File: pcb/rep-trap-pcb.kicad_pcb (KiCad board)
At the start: 2 copper layers, 141.9 x 37 mm, 39 parts, among them J1 USB4105-GF-A, J2 S2B-PH-K, U1 VL53L4CDV0DH/1, U2 VL53L4CDV0DH/1, U3 VL53L4CDV0DH/1, U4 VL53L4CDV0DH/1, U5 RP2040, U6 MCP73831/OT, U8 AP2112K-3.3

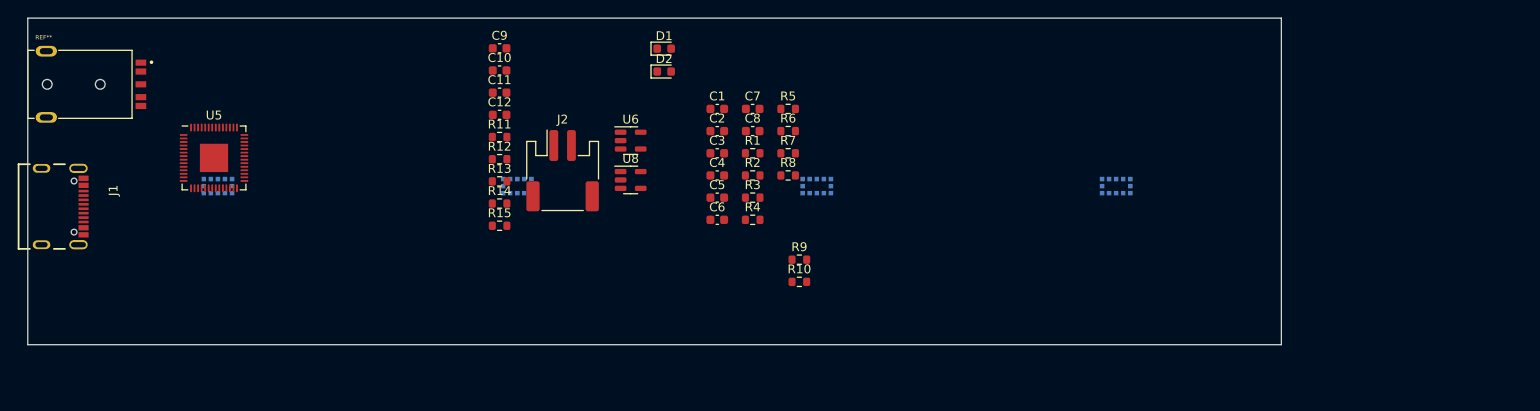
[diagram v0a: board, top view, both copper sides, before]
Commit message: Added pcb design for first prototype
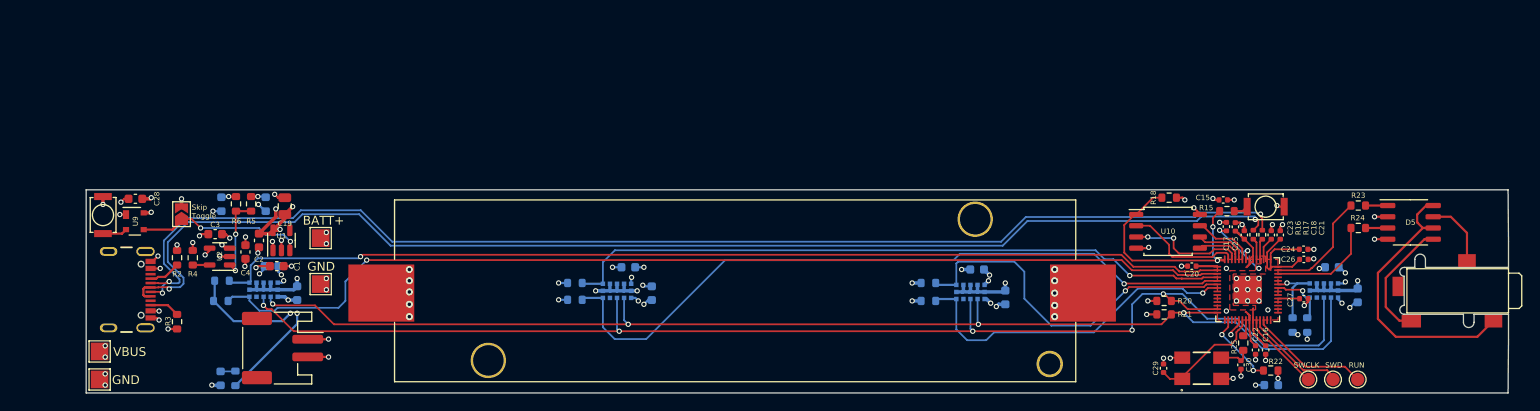
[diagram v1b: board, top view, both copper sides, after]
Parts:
- removed REF**: CUI_SJ-3541AS-SMT-TR-67, SJ-3541AS-SMT-TR-67:CUI_SJ-3541AS-SMT-TR-67
- added BT1: Battery_Cell, 1042P:1042P, F.Cu at (142.6, 90.9)
- added C15: 100n, Capacitor_SMD:C_0402_1005Metric, F.Cu at (197.9, 80.4)
- added C16: 0.1uF, Capacitor_SMD:C_0402_1005Metric, F.Cu at (202.7, 97.4)
- added C17: 0.1uF, Capacitor_SMD:C_0402_1005Metric, F.Cu at (198.2, 83.4)
- added C18: 1uF, Capacitor_SMD:C_0402_1005Metric, F.Cu at (203.3, 84.4)
- added C19: 10uF, Capacitor_SMD:C_0805_2012Metric, F.Cu at (91.7, 81.1)
- added C20: 0.1uF, Capacitor_SMD:C_0402_1005Metric, F.Cu at (194.3, 87.9)
- added C21: 1uF, Capacitor_SMD:C_0402_1005Metric, F.Cu at (204.3, 84.4)
- added C22: 0.1uF, Capacitor_SMD:C_0402_1005Metric, F.Cu at (201.5, 97.4)
- added C23: 0.1uF, Capacitor_SMD:C_0402_1005Metric, F.Cu at (200.3, 84.4)
- added C24: 0.1uF, Capacitor_SMD:C_0402_1005Metric, F.Cu at (207.0, 86.0)
- added C25: 0.1uF, Capacitor_SMD:C_0402_1005Metric, F.Cu at (199.3, 83.4)
- added C26: 0.1uF, Capacitor_SMD:C_0402_1005Metric, F.Cu at (207.0, 87.1)
- added C27: 0.1uF, Capacitor_SMD:C_0402_1005Metric, F.Cu at (207.0, 91.6)
- added C28: 0.1uF, Capacitor_SMD:C_0603_1608Metric, F.Cu at (74.8, 80.3)
- added C29: 27p, Capacitor_SMD:C_0402_1005Metric, F.Cu at (191.1, 99.4)
- added C30: 27p, Capacitor_SMD:C_0402_1005Metric, F.Cu at (199.9, 99.1)
- added D3: GREEN, LED_SMD:LED_0603_1608Metric, B.Cu at (84.5, 80.9)
- added D4: LED_RED, LED_SMD:LED_0603_1608Metric, B.Cu at (203.3, 101.3)
- added D5: ELD207, Package_SO:SO-8_3.9x4.9mm_P1.27mm, F.Cu at (219.1, 82.9)
- added J3: USB4105-GF-A, USB4105-GF-A:GCT_USB4105-GF-A, F.Cu at (71.8, 90.5)
- added J4: VBUS, TestPoint:TestPoint_Pad_2.0x2.0mm, F.Cu at (70.7, 97.5)
- added J5: SJ2-25773B-SMT-TR, SJ-25773B-SMT:CUI_SJ2-25773B-SMT-TR, F.Cu at (224.4, 90.7)
- added J6: S2B-PH-K/DNP, Connector_JST:JST_PH_S2B-PH-SM4-TB_1x02-1MP_P2.00mm_Horizontal, F.Cu at (91.4, 97.2)
- added J7: GND, TestPoint:TestPoint_Pad_2.0x2.0mm, F.Cu at (70.7, 100.7)
- added JP1: SolderJumper_2_Open, Jumper:SolderJumper-2_P1.3mm_Open_TrianglePad1.0x1.5mm, F.Cu at (80.0, 82.0)
- added R16: 27, Resistor_SMD:R_0402_1005Metric, F.Cu at (201.3, 84.3)
- added R17: 27, Resistor_SMD:R_0402_1005Metric, F.Cu at (202.3, 84.3)
- added R18: 10k/DNP, Resistor_SMD:R_0603_1608Metric, F.Cu at (191.8, 80.1)
- added R20: 10k, Resistor_SMD:R_0603_1608Metric, F.Cu at (191.2, 91.8)
- added R21: 10k, Resistor_SMD:R_0603_1608Metric, F.Cu at (191.2, 93.3)
- added R22: 1k, Resistor_SMD:R_0603_1608Metric, F.Cu at (203.3, 99.7)
- added R23: 220, Resistor_SMD:R_0603_1608Metric, F.Cu at (213.2, 81.0)
- added R24: 220, Resistor_SMD:R_0603_1608Metric, F.Cu at (213.2, 83.6)
- added R25: 1k, Resistor_SMD:R_0603_1608Metric, F.Cu at (200.2, 96.6)
- added SW1: SW_Push, SKRKAEE020:SKRKAEE020, F.Cu at (202.7, 81.2)
- added SW2: SW_Push, SKRKAEE020:SKRKAEE020, F.Cu at (71.1, 82.1)
- added TP1: TP_SWCLK, TestPoint:TestPoint_Pad_D1.5mm, F.Cu at (207.5, 100.7)
- added TP2: TP_SWD, TestPoint:TestPoint_Pad_D1.5mm, F.Cu at (210.3, 100.7)
- added TP3: TestPoint, TestPoint:TestPoint_Pad_D1.5mm, F.Cu at (213.1, 100.7)
- added U10: W25Q128JVS, Package_SO:SOIC-8_5.23x5.23mm_P1.27mm, F.Cu at (191.6, 83.9)
- added U9: MAX6816, Package_TO_SOT_SMD:SOT-143, F.Cu at (74.7, 82.8)
- added Y3: ABMM2-12.000MHZ-E2-T, ABMM2-12.000MHZ-E2-T:ABMM2, F.Cu at (195.5, 99.4)
- C1, C2: value 4.7uF -> 1µF
- C10, C9: value 1µF -> 4.7uF; moved to B.Cu
- C11, C12: value 10µF -> 0.1uF; moved to B.Cu
- C3: value 4.7uF -> 10µF
- C4: value 0.1uF -> 10µF
- C5, C6: value 0.1uF -> 4.7uF; moved to B.Cu
- C7: value 4.7uF -> 0.1uF; moved to B.Cu
- C8, R10, R7, R8, R9: moved to B.Cu
- D1: value RED -> LED_Small; moved to B.Cu
- D2: value GREEN -> RED; moved to B.Cu
- J1: value USB4105-GF-A -> BATT+; footprint USB4105-GF-A:GCT_USB4105-GF-A -> TestPoint:TestPoint_Pad_2.0x2.0mm
- J2: value S2B-PH-K -> GND; footprint Connector_JST:JST_PH_S2B-PH-SM4-TB_1x02-1MP_P2.00mm_Horizontal -> TestPoint:TestPoint_Pad_2.0x2.0mm
- R1: value 10k -> 1k; moved to B.Cu
- R11: value 2k -> 10k; moved to B.Cu
- R12, R13: value 1k -> 10k; moved to B.Cu
- R14: value 5k1 -> 10k; moved to B.Cu
- R15: value 5k1 -> 1k
- R2, R3: value 10k -> 5k1
- R4: value 10k -> 2k
- R5, R6: value 10k -> 1k
- U1: value VL53L4CDV0DH/1 -> AP2112K-3.3; footprint VL53L4CD:LGA12_STM -> Package_TO_SOT_SMD:SOT-23-5; moved to F.Cu
- U2: value VL53L4CDV0DH/1 -> MCP73831/OT; footprint VL53L4CD:LGA12_STM -> Package_TO_SOT_SMD:SOT-23-5; moved to F.Cu
- U5: value RP2040 -> VL53L4CDV0DH/1; footprint Package_DFN_QFN:QFN-56-1EP_7x7mm_P0.4mm_EP3.2x3.2mm -> VL53L4CD:LGA12_STM; moved to B.Cu
- U6: value MCP73831/OT -> VL53L4CDV0DH/1; footprint Package_TO_SOT_SMD:SOT-23-5 -> VL53L4CD:LGA12_STM; moved to B.Cu
- U8: value AP2112K-3.3 -> RP2040; footprint Package_TO_SOT_SMD:SOT-23-5 -> Package_DFN_QFN:QFN-56-1EP_7x7mm_P0.4mm_EP3.2x3.2mm
- moved U5 126.5 mm to (209.3, 90.6), turned to 90 degrees
- moved C9 101.0 mm to (213.1, 91.2), turned to 90 degrees
- moved C11 96.2 mm to (210.2, 88.0), turned to 180 degrees
- moved U1 94.7 mm to (91.3, 85.0)
- moved R12 93.3 mm to (207.4, 94.6), turned to -90 degrees
- moved R11 92.2 mm to (205.7, 94.6), turned to -90 degrees
- moved R15 82.3 mm to (198.3, 81.7)
- moved U8 70.9 mm to (200.7, 90.6)
- moved U2 68.0 mm to (84.3, 86.8), turned to 180 degrees
- moved R3 66.6 mm to (79.5, 94.2), turned to 90 degrees
- moved R2 65.8 mm to (79.5, 86.9), turned to -90 degrees
- moved R10 65.5 mm to (84.5, 91.8), turned to 180 degrees
- moved R9 65.4 mm to (84.6, 89.5), turned to 180 degrees
- moved R1 63.8 mm to (86.1, 100.6), turned to -90 degrees
- moved R4 63.5 mm to (81.3, 86.9), turned to 90 degrees
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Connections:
- C1 pad 1: +3.3V -> +BATT
- C10 pad 1: +3V3 -> +3.3V
- C11 pad 1: /PSU and charging/VBUS -> +3.3V
- C12 pad 1: /PSU and charging/VBAT -> +3.3V
- C3 pad 1: +3.3V -> VBUS
- C4 pad 1: +3.3V -> +BATT
- C9 pad 1: /PSU and charging/VBAT -> +3.3V
- D1 pad 1: Net-(D1-K) -> GND
- D1 pad 2: /PSU and charging/VBUS -> Net-(D1-A)
- D2 pad 1: GND -> Net-(D2-K)
- D2 pad 2: Net-(D2-A) -> +BATT
- J2 pad 1: /PSU and charging/VBAT -> GND
- R1 pad 1: /ToF Array/XSHUT_VL53_2 -> Net-(D1-A)
- R10 pad 1: /MCU/SCL -> /main/MCU/INT_VL53_1
- R11 pad 1: Net-(U6-PROG) -> /main/MCU/XSHUT_VL53_4
- R11 pad 2: GND -> +3.3V
- R12 pad 1: /PSU and charging/STAT -> /main/MCU/INT_VL53_4
- R12 pad 2: Net-(D1-K) -> +3.3V
- R13 pad 1: /PSU and charging/STAT -> /main/MCU/XSHUT_VL53_3
- R13 pad 2: Net-(D2-A) -> +3.3V
- R14 pad 1: GND -> /main/MCU/INT_VL53_3
- R14 pad 2: Net-(J1-CC1) -> +3.3V
- R15 pad 1: GND -> /main/MCU/QSPI_SS
- R15 pad 2: Net-(J1-CC2) -> Net-(R15-Pad2)
- R2 pad 1: /ToF Array/INT_VL53_2 -> GND
- R2 pad 2: +3.3V -> Net-(J3-CC1)
- R3 pad 1: /ToF Array/XSHUT_VL53_3 -> GND
- R3 pad 2: +3.3V -> Net-(J3-CC2)
- R4 pad 1: /ToF Array/INT_VL53_3 -> Net-(U2-PROG)
- R4 pad 2: +3.3V -> GND
- R5 pad 1: /ToF Array/XSHUT_VL53_1 -> /main/PSU and charging/STAT
- R5 pad 2: +3.3V -> Net-(D2-K)
- R6 pad 1: /ToF Array/INT_VL53_1 -> /main/PSU and charging/STAT
- R6 pad 2: +3.3V -> Net-(D3-A)
- R7 pad 1: /ToF Array/XSHUT_VL53_4 -> /main/MCU/XSHUT_VL53_2
- R8 pad 1: /ToF Array/INT_VL53_4 -> /main/MCU/INT_VL53_2
- R9 pad 1: /MCU/SDA -> /main/MCU/XSHUT_VL53_1
- U1 pad 1: +3.3V -> +BATT
- U1 pad 3: GND -> /main/ENABLE
- U1 pad 4: GND -> unconnected-(U1-NC-Pad4)
- U1 pad 5: /ToF Array/XSHUT_VL53_2 -> +3.3V
- U2 pad 1: +3.3V -> /main/PSU and charging/STAT
- U2 pad 3: GND -> +BATT
- U2 pad 4: GND -> VBUS
- U2 pad 5: /ToF Array/XSHUT_VL53_3 -> Net-(U2-PROG)
- U3 pad 10: /ToF Array/SCL -> /main/MCU/SCL
- U3 pad 5: /ToF Array/XSHUT_VL53_1 -> /main/MCU/XSHUT_VL53_2
- U3 pad 7: /ToF Array/INT_VL53_1 -> /main/MCU/INT_VL53_2
- U3 pad 9: /ToF Array/SDA -> /main/MCU/SDA
- U4 pad 10: /ToF Array/SCL -> /main/MCU/SCL
- U4 pad 5: /ToF Array/XSHUT_VL53_4 -> /main/MCU/XSHUT_VL53_1
- U4 pad 7: /ToF Array/INT_VL53_4 -> /main/MCU/INT_VL53_1
- U4 pad 9: /ToF Array/SDA -> /main/MCU/SDA
- U5 pad 1: Net-(U5-IOVDD-Pad1) -> +3.3V
- U5 pad 10: Net-(U5-IOVDD-Pad1) -> /main/MCU/SCL
- U5 pad 11: unconnected-(U5-GPIO8-Pad11) -> +3.3V
- U5 pad 12: unconnected-(U5-GPIO9-Pad12) -> GND
- U5 pad 2: unconnected-(U5-GPIO0-Pad2) -> GND
- U5 pad 3: unconnected-(U5-GPIO1-Pad3) -> GND
- U5 pad 4: unconnected-(U5-GPIO2-Pad4) -> GND
- U5 pad 5: unconnected-(U5-GPIO3-Pad5) -> /main/MCU/XSHUT_VL53_4
- U5 pad 6: unconnected-(U5-GPIO4-Pad6) -> GND
- U5 pad 7: unconnected-(U5-GPIO5-Pad7) -> /main/MCU/INT_VL53_4
- U5 pad 9: unconnected-(U5-GPIO7-Pad9) -> /main/MCU/SDA
- U6 pad 1: /PSU and charging/STAT -> +3.3V
- U6 pad 3: /PSU and charging/VBAT -> GND
- U6 pad 4: /PSU and charging/VBUS -> GND
- U6 pad 5: Net-(U6-PROG) -> /main/MCU/XSHUT_VL53_3
- U8 pad 1: /PSU and charging/VBAT -> +3.3V
- U8 pad 2: GND -> /main/MCU/XSHUT_VL53_1
- U8 pad 3: /PSU and charging/EN -> /main/MCU/INT_VL53_1
- U8 pad 4: unconnected-(U8-NC-Pad4) -> /main/MCU/XSHUT_VL53_2
- U8 pad 5: +3V3 -> /main/MCU/INT_VL53_2
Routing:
- net /main/MCU/SDA: track 0.00 -> 147.6 mm, vias 0 -> 5
- net /main/USB_D-: track 0.00 -> 142.4 mm, vias 0 -> 3
- net /main/USB_D+: track 0.00 -> 141.2 mm, vias 0 -> 2
- net /main/MCU/SCL: track 0.00 -> 139.1 mm, vias 0 -> 4
- net /main/MCU/INT_VL53_1: track 0.00 -> 117.5 mm, vias 0 -> 1
- net /main/MCU/XSHUT_VL53_1: track 0.00 -> 115.1 mm, vias 0 -> 1
- net +3.3V: track 0.00 -> 89.1 mm, vias 0 -> 34
- net /main/MCU/INT_VL53_2: track 0.00 -> 81.4 mm, vias 0 -> 1
- net GND: track 0.00 -> 78.3 mm, vias 0 -> 66
- net /main/MCU/XSHUT_VL53_2: track 0.00 -> 76.3 mm, vias 0 -> 1
- net /main/MCU/XSHUT_VL53_3: track 0.00 -> 41.2 mm, vias 0 -> 1
- net /main/MCU/INT_VL53_3: track 0.00 -> 38.8 mm, vias 0 -> 1
- net Net-(D5-COLLECTOR_1): track 0.00 -> 33.4 mm
- net /main/MCU/QSPI_SS: track 0.00 -> 26.8 mm, vias 0 -> 2
- net /main/ENABLE: track 0.00 -> 19.2 mm, vias 0 -> 2
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- added copper zone on F.Cu, net +1V1
- added copper zone on F.Cu, net +3.3V
- added copper zone on In1.Cu, net +3.3V
- added copper zone on In1.Cu, net +BATT
- added copper zone on In2.Cu, net GND
- added copper zone on In1.Cu, net VBUS
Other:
- board size 141.9 x 37 mm -> 161 x 23 mm
- copper layers 2 -> 4
- board text added: "BATT+"
- board text added: "CHG"
- board text added: "DBG"
- board text added: "GND"
- board text added: "PWR"
- board text added: "RDY"
- board text added: "RUN"
- board text added: "SWCLK"
- board text added: "SWD"
- board text added: "Skip Toggle"
- board text added: "VBUS"

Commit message: Added Logo + Revision + generated Bom
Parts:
- added G***: LOGO, LOGO, B.Cu at (150.0, 97.7)
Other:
- board text added: "Rep Trap - Rev0.1 Prototype"

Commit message: Refactored details component namings + bom excludings
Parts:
- BT1: value Battery_Cell -> 1042P
- C10, C5, C6, C9: value 4.7uF -> 4.7µF
- C11, C12, C16, C17, C20, C22, C23, C24, C25, C26, C27, C28, C7, C8: value 0.1uF -> 0.1µF
- C15: value 100n -> 0.1µF
- C18, C21: value 1uF -> 1µF
- C19: value 10uF -> 10µF
- C29, C30: value 27p -> 27pF
- D1: value LED_Small -> LED_RED
- D2: value RED -> LED_RED
- D3: value GREEN -> LED_GREEN
- R20, R21: value 10k -> 2.2k
- SW1, SW2: value SW_Push -> SKRKAEE020
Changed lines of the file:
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@@
         (effects (font (size 0.6 0.6) (thickness 0.15)))
     )
-    (fp_text value "0.1uF" (at 0 1.16 90) (layer "F.Fab")
+    (fp_text value "0.1µF" (at 0 1.16 90) (layer "F.Fab")
         (effects (font (size 1 1) (thickness 0.15)))
     )
@@
     (property "Sheetfile" "mcu.kicad_sch")
     (property "Sheetname" "MCU")
+    (property "exclude_from_bom" "")
     (property "ki_description" "test point")
     (property "ki_keywords" "test point tp")
@@
         (effects (font (size 0.6 0.6) (thickness 0.15)))
     )
-    (fp_text value "0.1uF" (at 0 1.43) (layer "F.Fab")
+    (fp_text value "0.1µF" (at 0 1.43) (layer "F.Fab")
         (effects (font (size 1 1) (thickness 0.15)))
     )
@@
         (effects (font (size 0.6 0.6) (thickness 0.15)))
     )
-    (fp_text value "0.1uF" (at 0 1.16) (layer "F.Fab")
+    (fp_text value "0.1µF" (at 0 1.16) (layer "F.Fab")
         (effects (font (size 1 1) (thickness 0.15)))
     )
@@
         (effects (font (size 0.6 0.6) (thickness 0.15)))
     )
-    (fp_text value "1uF" (at 0 1.16 90) (layer "F.Fab")
+    (fp_text value "1µF" (at 0 1.16 90) (layer "F.Fab")
         (effects (font (size 1 1) (thickness 0.15)))
     )
@@
         (effects (font (size 0.6 0.6) (thickness 0.15)))
     )
-    (fp_text value "100n" (at 0 1.16) (layer "F.Fab")
+    (fp_text value "0.1µF" (at 0 1.16) (layer "F.Fab")
         (effects (font (size 1 1) (thickness 0.15)))
     )
@@
         (effects (font (size 0.6 0.6) (thickness 0.15)))
     )
-    (fp_text value "0.1uF" (at 0 1.16) (layer "F.Fab")
+    (fp_text value "0.1µF" (at 0 1.16) (layer "F.Fab")
         (effects (font (size 1 1) (thickness 0.15)))
     )
@@
         (effects (font (size 0.6 0.6) (thickness 0.15)))
     )
-    (fp_text value "0.1uF" (at 0 1.16) (layer "F.Fab")
+    (fp_text value "0.1µF" (at 0 1.16) (layer "F.Fab")
         (effects (font (size 1 1) (thickness 0.15)))
     )
@@
         (effects (font (size 0.6 0.6) (thickness 0.15)))
     )
-    (fp_text value "1uF" (at 0 1.16 90) (layer "F.Fab")
+    (fp_text value "1µF" (at 0 1.16 90) (layer "F.Fab")
         (effects (font (size 1 1) (thickness 0.15)))
     )
@@
         (effects (font (size 0.6 0.6) (thickness 0.15)))
     )
-    (fp_text value "27p" (at 0 1.16 90) (layer "F.Fab")
+    (fp_text value "27pF" (at 0 1.16 90) (layer "F.Fab")
         (effects (font (size 1 1) (thickness 0.15)))
     )
@@
     (property "Sheetfile" "psu_charging.kicad_sch")
     (property "Sheetname" "PSU and charging")
+    (property "exclude_from_bom" "")
     (property "ki_description" "Solder Jumper, 2-pole, open")
     (property "ki_keywords" "solder jumper SPST")
-    (attr exclude_from_pos_files)
+    (attr exclude_from_pos_files exclude_from_bom)
     (fp_text reference "JP1" (at 0 -1.8 90) (layer "F.SilkS") hide
         (effects (font (size 1 1) (thickness 0.15)))
@@
         (effects (font (size 1 1) (thickness 0.15)))
     )
-    (fp_text value "Battery_Cell" (at 0 3.683 unlocked) (layer "F.Fab")
+    (fp_text value "1042P" (at 0 3.683 unlocked) (layer "F.Fab")
         (effects (font (size 1 1) (thickness 0.15)))
     )
@@
         (effects (font (size 0.6 0.6) (thickness 0.15)))
     )
-    (fp_text value "0.1uF" (at 0 1.16 90) (layer "F.Fab")
+    (fp_text value "0.1µF" (at 0 1.16 90) (layer "F.Fab")
         (effects (font (size 1 1) (thickness 0.15)))
     )
@@
         (effects (font (size 0.6 0.6) (thickness 0.15)))
     )
-    (fp_text value "10uF" (at 0 1.68 90) (layer "F.Fab")
+    (fp_text value "10µF" (at 0 1.68 90) (layer "F.Fab")
         (effects (font (size 1 1) (thickness 0.15)))
     )
@@
         (effects (font (size 0.6 0.6) (thickness 0.15)))
     )
-    (fp_text value "27p" (at 0 1.16 90) (layer "F.Fab")
+    (fp_text value "27pF" (at 0 1.16 90) (layer "F.Fab")
         (effects (font (size 1 1) (thickness 0.15)))
     )
@@
         (effects (font (size 0.6 0.6) (thickness 0.15)))
     )
-    (fp_text value "0.1uF" (at 0 1.16 90) (layer "F.Fab")
+    (fp_text value "0.1µF" (at 0 1.16 90) (layer "F.Fab")
         (effects (font (size 1 1) (thickness 0.15)))
     )
@@
         (effects (font (size 0.6 0.6) (thickness 0.15)))
     )
-    (fp_text value "0.1uF" (at 0 1.16) (layer "F.Fab")
+    (fp_text value "0.1µF" (at 0 1.16) (layer "F.Fab")
         (effects (font (size 1 1) (thickness 0.15)))
     )
@@
         (effects (font (size 0.6 0.6) (thickness 0.15)))
     )
-    (fp_text value "10k" (at 0 1.43) (layer "F.Fab")
+    (fp_text value "2.2k" (at 0 1.43) (layer "F.Fab")
         (effects (font (size 1 1) (thickness 0.15)))
     )
@@
         (effects (font (size 1 1) (thickness 0.15)))
     )
-    (fp_text value "SW_Push" (at 0 -2.2987 90) (layer "F.Fab")
+    (fp_text value "SKRKAEE020" (at 0 -2.2987 90) (layer "F.Fab")
         (effects (font (size 1 1) (thickness 0.15)))
     )
@@
         (effects (font (size 0.6 0.6) (thickness 0.15)))
     )
-    (fp_text value "10k" (at 0 1.43) (layer "F.Fab")
+    (fp_text value "2.2k" (at 0 1.43) (layer "F.Fab")
         (effects (font (size 1 1) (thickness 0.15)))
     )
@@
         (effects (font (size 0.6 0.6) (thickness 0.15)))
     )
-    (fp_text value "0.1uF" (at 0 1.16 90) (layer "F.Fab")
+    (fp_text value "0.1µF" (at 0 1.16 90) (layer "F.Fab")
         (effects (font (size 1 1) (thickness 0.15)))
     )
@@
     (property "Sheetfile" "psu_charging.kicad_sch")
     (property "Sheetname" "PSU and charging")
+    (property "exclude_from_bom" "")
     (property "ki_description" "Generic connector, single row, 01x02, script generated")
     (property "ki_keywords" "connector")
@@
     (property "Sheetfile" "mcu.kicad_sch")
     (property "Sheetname" "MCU")
+    (property "exclude_from_bom" "")
     (property "ki_description" "test point")
     (property "ki_keywords" "test point tp")
@@
     (property "Sheetfile" "mcu.kicad_sch")
     (property "Sheetname" "MCU")
+    (property "exclude_from_bom" "")
     (property "ki_description" "test point")
     (property "ki_keywords" "test point tp")
@@
         (effects (font (size 1 1) (thickness 0.15)))
     )
-    (fp_text value "SW_Push" (at 0 -2.2987) (layer "F.Fab")
+    (fp_text value "SKRKAEE020" (at 0 -2.2987) (layer "F.Fab")
         (effects (font (size 1 1) (thickness 0.15)))
     )
@@
         (effects (font (size 0.6 0.6) (thickness 0.15)))
     )
-    (fp_text value "0.1uF" (at 0 1.16 90) (layer "F.Fab")
+    (fp_text value "0.1µF" (at 0 1.16 90) (layer "F.Fab")
         (effects (font (size 1 1) (thickness 0.15)))
     )
@@
         (effects (font (size 0.6 0.6) (thickness 0.15)) (justify mirror))
     )
-    (fp_text value "0.1uF" (at 0 -1.43) (layer "B.Fab")
+    (fp_text value "0.1µF" (at 0 -1.43) (layer "B.Fab")
         (effects (font (size 1 1) (thickness 0.15)) (justify mirror))
     )
@@
         (effects (font (size 0.6 0.6) (thickness 0.15)) (justify mirror))
     )
-    (fp_text value "4.7uF" (at 0 -1.43 90) (layer "B.Fab")
+    (fp_text value "4.7µF" (at 0 -1.43 90) (layer "B.Fab")
         (effects (font (size 1 1) (thickness 0.15)) (justify mirror))
     )
@@
         (effects (font (size 0.6 0.6) (thickness 0.15)) (justify mirror))
     )
-    (fp_text value "0.1uF" (at -0.495 -1.27 90) (layer "B.Fab")
+    (fp_text value "0.1µF" (at -0.495 -1.27 90) (layer "B.Fab")
         (effects (font (size 1 1) (thickness 0.15)) (justify mirror))
     )
@@
         (effects (font (size 0.6 0.6) (thickness 0.15)) (justify mirror))
     )
-    (fp_text value "0.1uF" (at 0 -1.43) (layer "B.Fab")
+    (fp_text value "0.1µF" (at 0 -1.43) (layer "B.Fab")
         (effects (font (size 1 1) (thickness 0.15)) (justify mirror))
     )
@@
         (effects (font (size 0.6 0.6) (thickness 0.15)) (justify mirror))
     )
-    (fp_text value "0.1uF" (at 0 -1.43) (layer "B.Fab")
+    (fp_text value "0.1µF" (at 0 -1.43) (layer "B.Fab")
         (effects (font (size 1 1) (thickness 0.15)) (justify mirror))
     )
@@
         (effects (font (size 0.6 0.6) (thickness 0.15)) (justify mirror))
     )
-    (fp_text value "LED_Small" (at 0 -1.43 90) (layer "B.Fab")
+    (fp_text value "LED_RED" (at 0 -1.43 90) (layer "B.Fab")
         (effects (font (size 1 1) (thickness 0.15)) (justify mirror))
     )
@@
         (effects (font (size 1 1) (thickness 0.15)) (justify mirror))
     )
-    (fp_text value "RED" (at 0 -1.43 90) (layer "B.Fab")
+    (fp_text value "LED_RED" (at 0 -1.43 90) (layer "B.Fab")
         (effects (font (size 1 1) (thickness 0.15)) (justify mirror))
     )
@@
         (effects (font (size 1 1) (thickness 0.15)) (justify mirror))
     )
-    (fp_text value "GREEN" (at 0 -1.43 90) (layer "B.Fab")
+    (fp_text value "LED_GREEN" (at 0 -1.43 90) (layer "B.Fab")
         (effects (font (size 1 1) (thickness 0.15)) (justify mirror))
     )
@@
         (effects (font (size 0.6 0.6) (thickness 0.15)) (justify mirror))
     )
-    (fp_text value "4.7uF" (at 0 -1.43 90) (layer "B.Fab")
+    (fp_text value "4.7µF" (at 0 -1.43 90) (layer "B.Fab")
         (effects (font (size 1 1) (thickness 0.15)) (justify mirror))
     )
@@
         (effects (font (size 0.6 0.6) (thickness 0.15)) (justify mirror))
     )
-    (fp_text value "4.7uF" (at 0 -1.43) (layer "B.Fab")
+    (fp_text value "4.7µF" (at 0 -1.43) (layer "B.Fab")
         (effects (font (size 1 1) (thickness 0.15)) (justify mirror))
     )
@@
         (effects (font (size 0.6 0.6) (thickness 0.15)) (justify mirror))
     )
-    (fp_text value "4.7uF" (at 0 -1.43 90) (layer "B.Fab")
+    (fp_text value "4.7µF" (at 0 -1.43 90) (layer "B.Fab")
         (effects (font (size 1 1) (thickness 0.15)) (justify mirror))
     )

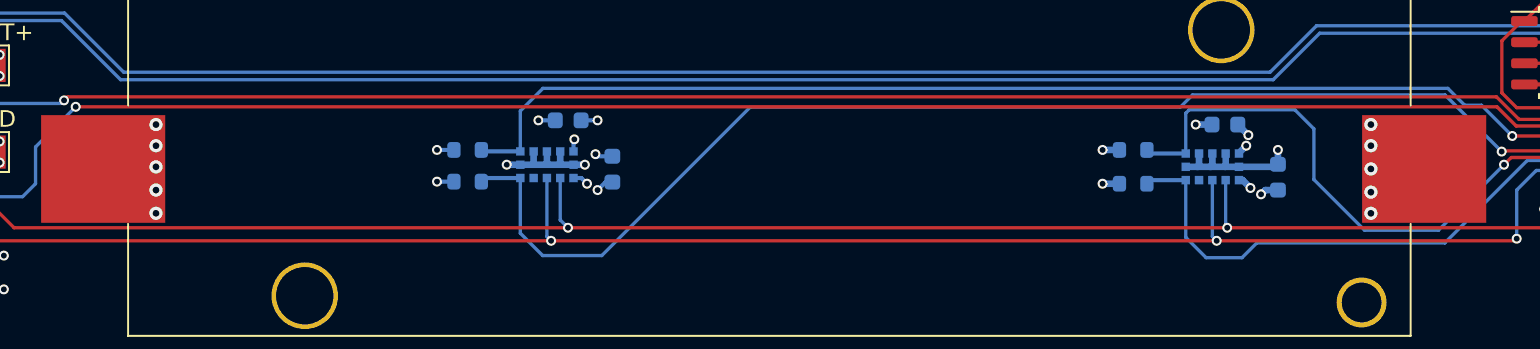
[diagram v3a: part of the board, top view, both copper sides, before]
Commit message: Moved via out of the pad
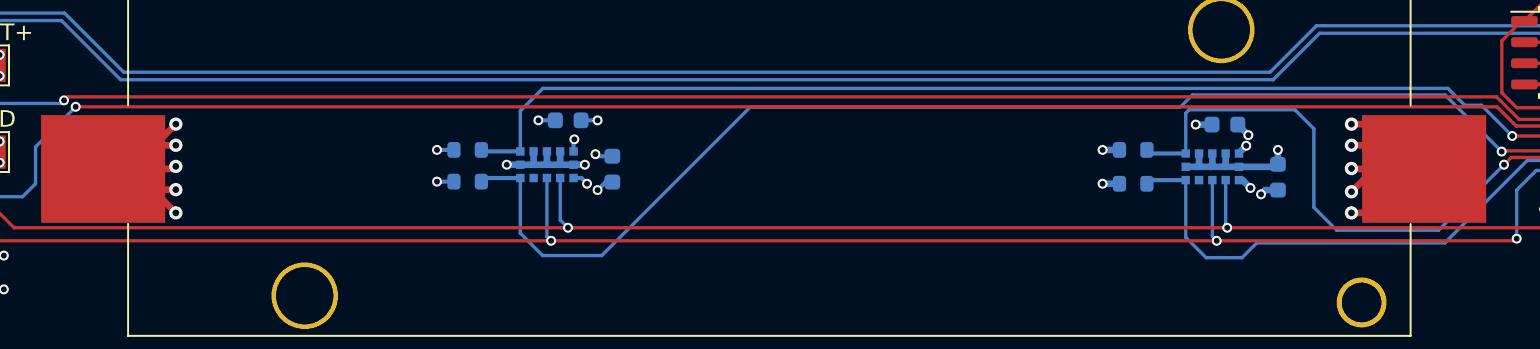
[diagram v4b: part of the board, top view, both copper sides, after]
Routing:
- net +BATT: track 12.0 -> 37.2 mm
- net GND: track 78.3 -> 103.5 mm
- net /main/MCU/XSHUT_VL53_3: track 41.2 -> 42.2 mm
